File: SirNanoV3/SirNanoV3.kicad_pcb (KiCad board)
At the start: 2 copper layers, 43.2 x 17.8 mm, 49 parts, among them J1 Conn_01x15, J2 Conn_01x15, U1 ATmega328PB-MU, U3 FT231XQ, Y1 20MHz

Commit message: Soldermask width adjusted
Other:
- rule solder_mask_min_width: 0.1 -> 0.05
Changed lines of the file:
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@@
   )
   (setup
-    (last_trace_width 0.25)
+    (last_trace_width 0.127)
     (user_trace_width 0.127)
     (user_trace_width 0.15)
@@
     (pad_drill 1)
     (pad_to_mask_clearance 0)
-    (solder_mask_min_width 0.1)
+    (solder_mask_min_width 0.05)
     (aux_axis_origin 0 0)
     (grid_origin 43.18 45.72)

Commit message: SirNanoR3 Update
20MHz Murata 3115 Resonator changed to 20MHz 3225_4P Resonator
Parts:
- removed C5: 10uF, Capacitor_SMD:C_0805_2012Metric
- added C10: 22pF, Capacitor_SMD:C_0603_1608Metric, F.Cu at (78.1, 38.0)
- added C12: 22pF, Capacitor_SMD:C_0603_1608Metric, F.Cu at (78.1, 32.5)
- Y1: footprint Crystal:Resonator_SMD_muRata_CSTxExxV-3Pin_3.0x1.1mm -> Crystal:Crystal_SMD_3225-4Pin_3.2x2.5mm
- moved C7 5.25 mm to (77.0, 40.8), turned to 270 degrees
- moved G*** 4.27 mm to (82.0, 36.8)
- moved G*** 3.43 mm to (62.4, 36.8)
- moved U2 2.37 mm to (79.7, 40.6)
- moved Y1 2.13 mm to (78.1, 35.2), turned to 90 degrees
- moved D3 1.22 mm to (83.9, 39.2)
- moved C8 1.10 mm to (83.9, 41.4)
- renumbered JST4-SH to J3, LDO to U2
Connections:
- Y1 pad 1: /X2 -> /X1
- Y1 pad 3: /X1 -> /X2
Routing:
- net VUSB: track 82.7 -> 76.9 mm
- net 3V3: track 79.1 -> 74.3 mm
- net /X1: track 3.65 -> 6.02 mm
- net D2: track 15.8 -> 14.0 mm
- net RESET: track 40.8 -> 39.2 mm, vias 2 -> 3
- net /X2: track 5.36 -> 3.98 mm
- net VIN: track 8.02 -> 6.93 mm

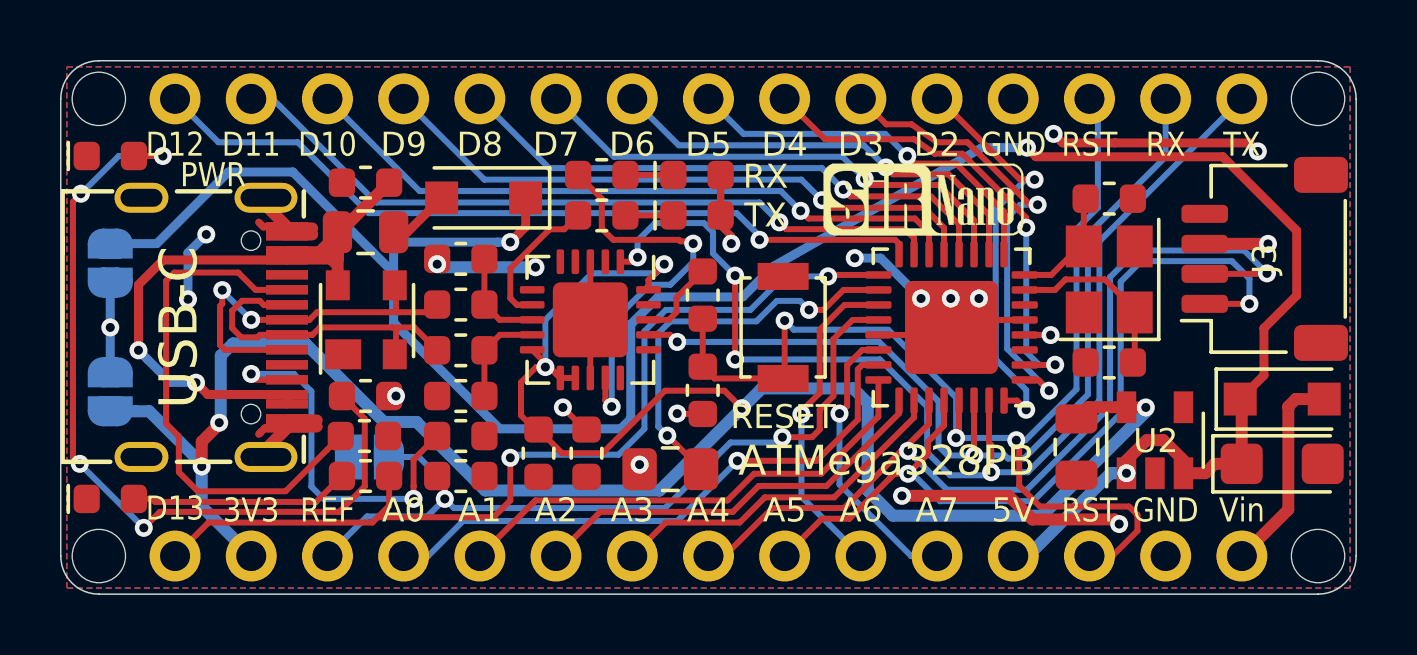
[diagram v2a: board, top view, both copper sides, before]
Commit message: Revision3.1
Layout Improved, PE0 and PE1 used for SirBlue Connector + USB-C 3D Renders Added and Pictures Updated
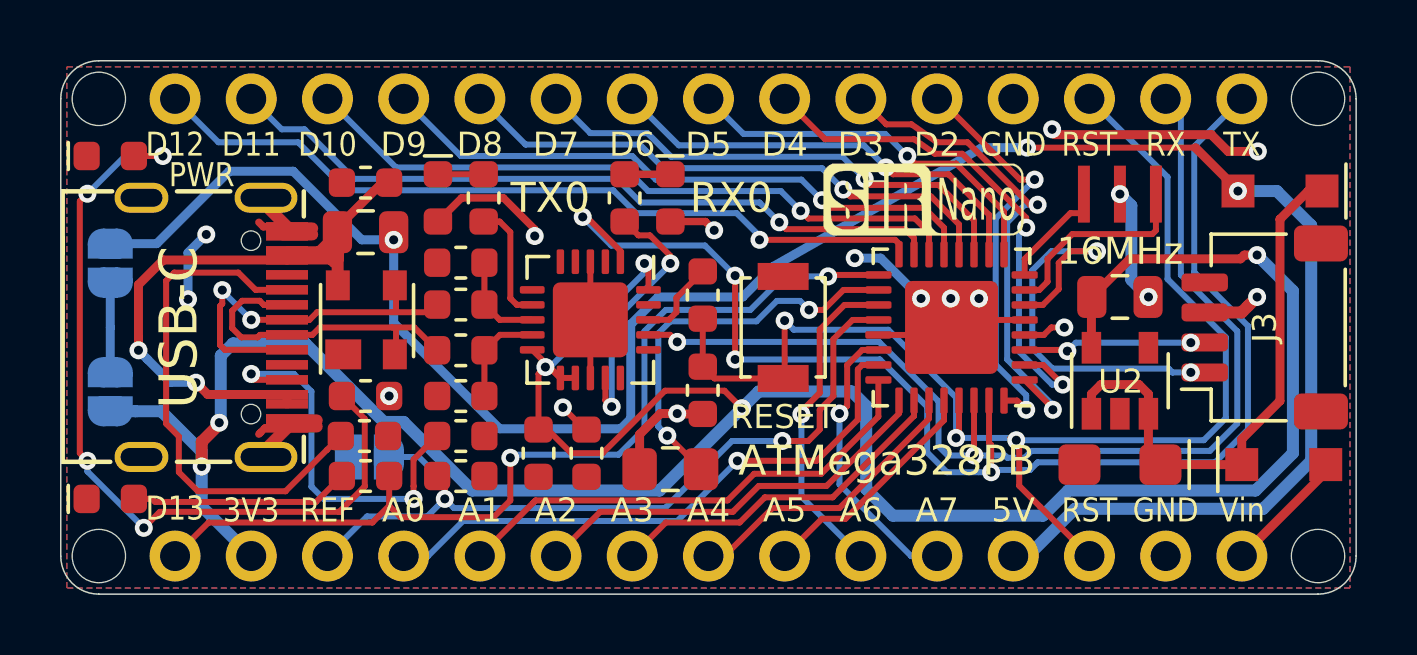
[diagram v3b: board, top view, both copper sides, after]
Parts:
- removed C10, C12: 22pF, Capacitor_SMD:C_0603_1608Metric
- G***: footprint logo:SirNano67x24 -> logo:Sir___67x24
- G***: footprint logo:SirBoard112x35 -> logo:SirBoard127x40
- Y1: value 20MHz -> 16MHz; footprint Crystal:Crystal_SMD_3225-4Pin_3.2x2.5mm -> Crystal:Resonator_SMD_muRata_CSTxExxV-3Pin_3.0x1.1mm
- moved D2 26.5 mm to (83.8, 32.3)
- moved TX0 8.66 mm to (55.8, 32.5), turned to 270 degrees
- moved C8 5.41 mm to (78.5, 41.4), turned to 180 degrees
- moved C7 5.21 mm to (78.5, 35.8), turned to 0 degrees
- moved R8 3.98 mm to (57.3, 32.5), turned to 90 degrees
- moved Y1 2.87 mm to (78.5, 32.4), turned to 0 degrees
- moved U2 2.30 mm to (78.5, 38.6)
- moved J3 2.29 mm to (83.3, 36.8)
- moved D3 2.18 mm to (83.9, 41.4)
- moved RX0 1.17 mm to (63.5, 32.5), turned to 270 degrees
- moved R4 1.08 mm to (62.0, 32.5), turned to 90 degrees
- moved G*** 0.19 mm to (54.9, 36.8)
- moved C2 0.13 mm to (56.5, 34.7)
- moved G*** 0.13 mm to (62.2, 36.8)
- renumbered RX to RX0, TX to TX0
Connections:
- C8 pad 1: VUSB -> /LDO_in
- D2 pad 1: VUSB -> /LDO_in
- D2 pad 2: Net-(D2-Pad2) -> VUSB
- D3 pad 1: VUSB -> /LDO_in
- F1 pad 1: Net-(D2-Pad2) -> VUSB
- J3 pad 1: A5 -> SCL1
- J3 pad 2: A4 -> SDA1
- U1 pad 3: Net-(U1-Pad3) -> SDA1
- U1 pad 6: Net-(U1-Pad6) -> SCL1
- U2 pad 1: VUSB -> /LDO_in
- U2 pad 3: VUSB -> /LDO_in
- Y1 pad 1: /X1 -> /X2
- Y1 pad 3: /X2 -> /X1
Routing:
- net A4: track 30.8 -> 9.85 mm, vias 2 -> 0
- net A5: track 28.4 -> 7.84 mm, vias 2 -> 0
- net /LDO_in: track 0.00 -> 18.5 mm
- net 3V3: track 74.3 -> 88.9 mm
- net SCL1: track 0.00 -> 14.3 mm, vias 0 -> 2
- net TX: track 38.7 -> 45.7 mm
- net SDA1: track 0.00 -> 5.67 mm, vias 0 -> 2
- net RX: track 30.9 -> 36.4 mm
- net VUSB: track 76.9 -> 71.8 mm
- net RX_LED: track 13.4 -> 8.86 mm
- net RESET: track 39.2 -> 42.7 mm
- net VIN: track 6.93 -> 4.21 mm
- net Net-(D2-Pad2): track 2.07 -> 0.00 mm
- net D4: track 16.3 -> 18.0 mm
- net VCC: track 25.3 -> 24.1 mm, vias 12 -> 9
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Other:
- board text added: "16MHz"
- board text added: "Nano"

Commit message: SirNano Silkscreen Widened
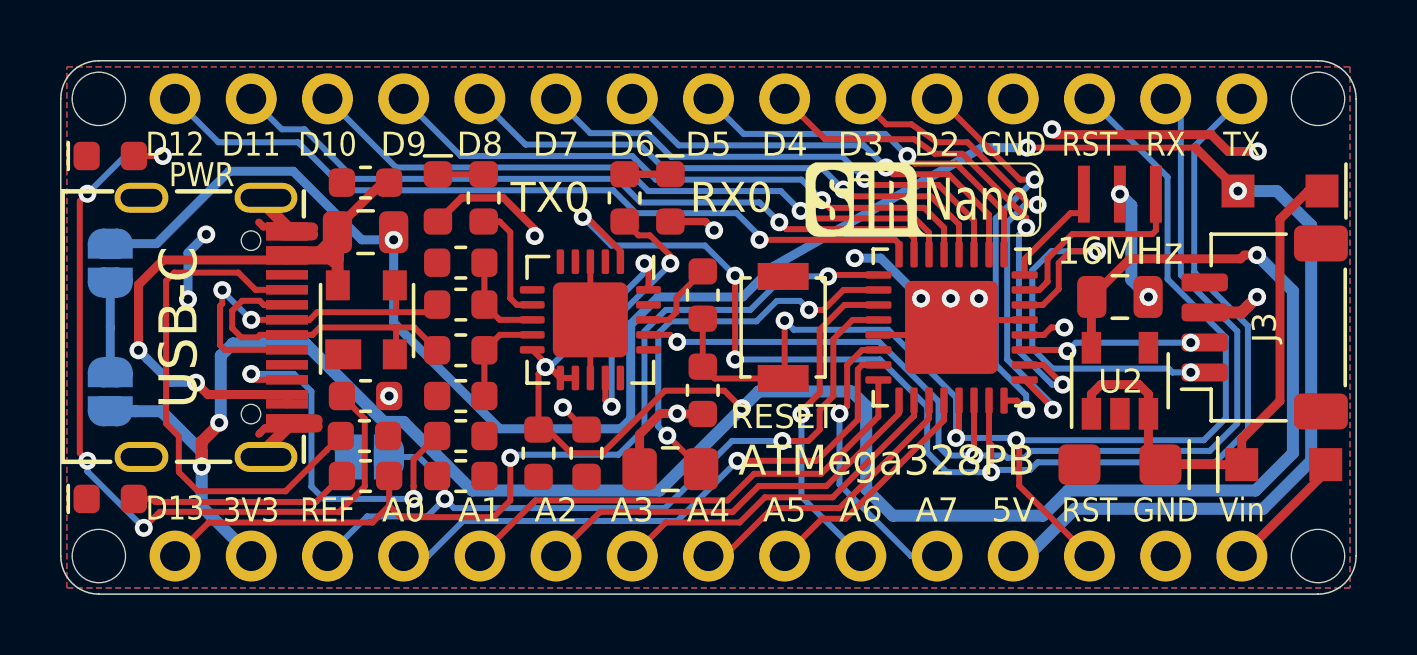
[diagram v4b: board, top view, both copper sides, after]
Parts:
- G***: footprint logo:Sir___67x24 -> logo:SirBoard79x25
